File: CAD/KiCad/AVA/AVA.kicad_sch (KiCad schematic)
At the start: 48 parts, among them J1 Conn_01x03_Pin, J10 Conn_01x04_Pin, J2 Conn_01x03_Pin, J3 Conn_01x03_Pin, J4 Conn_01x03_Pin, J5 Conn_01x02_Pin, J6 Conn_01x02_Pin, J7 Conn_01x02_Pin, J8 Conn_01x03_Pin, J9 Conn_01x03_Pin, U1 ESP32-C3-Super-Mini, U2 ESP32-DevKitC

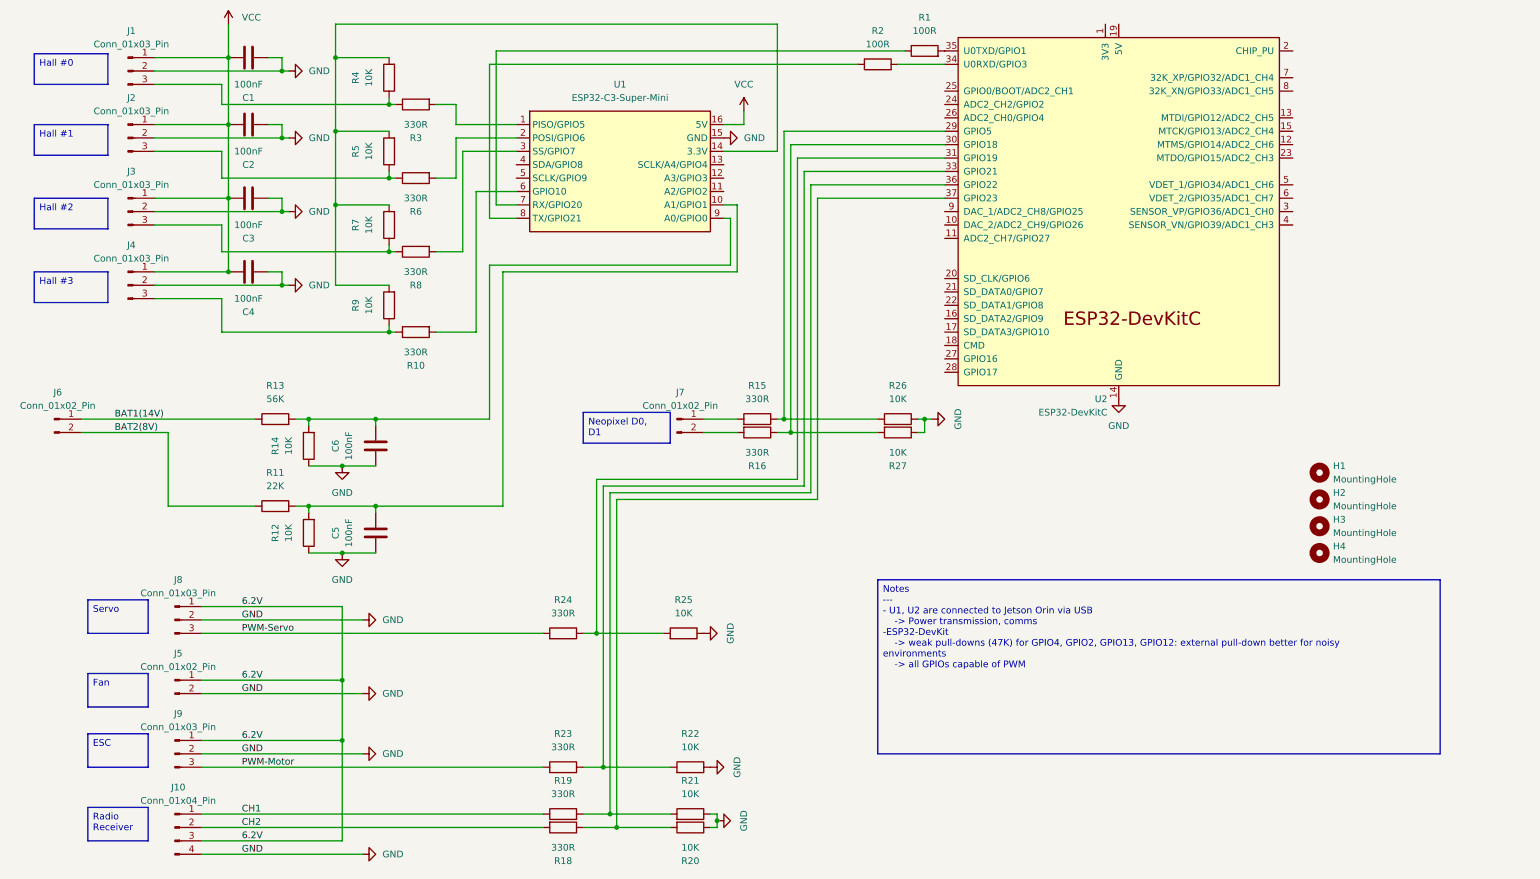
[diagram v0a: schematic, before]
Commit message: ESP32-DevKitC UART pins shared with usb, changing it to GPIO16/17. GPIO5 is strapping pin, changing pwm channels to GPIO4,18,19,20,21,22,23. GPIO4 in RTC-power-domain (touch sensor for deep-sleep mode, using it as normal PWM GPIO
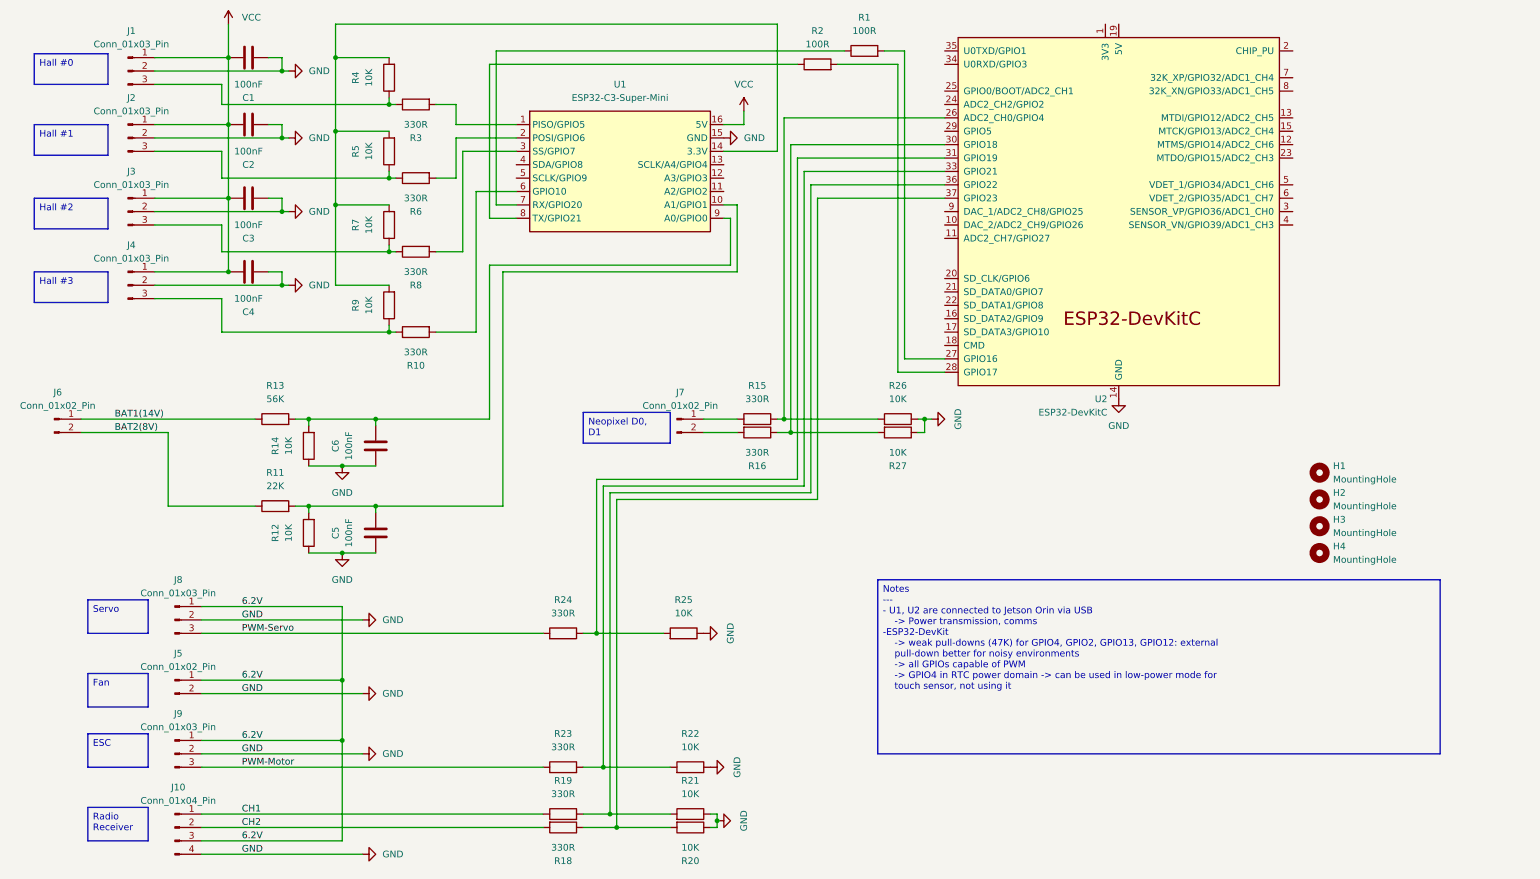
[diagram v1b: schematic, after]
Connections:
- net at R1.2: now also U2.27 (GPIO16); no longer U2.35 (U0TXD/GPIO1)
- net at R15.1, R26.2: now also U2.26 (ADC2_CH0/GPIO4); no longer U2.29 (GPIO5)
- net at R2.2: now also U2.28 (GPIO17); no longer U2.34 (U0RXD/GPIO3)
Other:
- moved on the sheet: R1, R2

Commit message: Added revision on pcb layout and updated 3D view
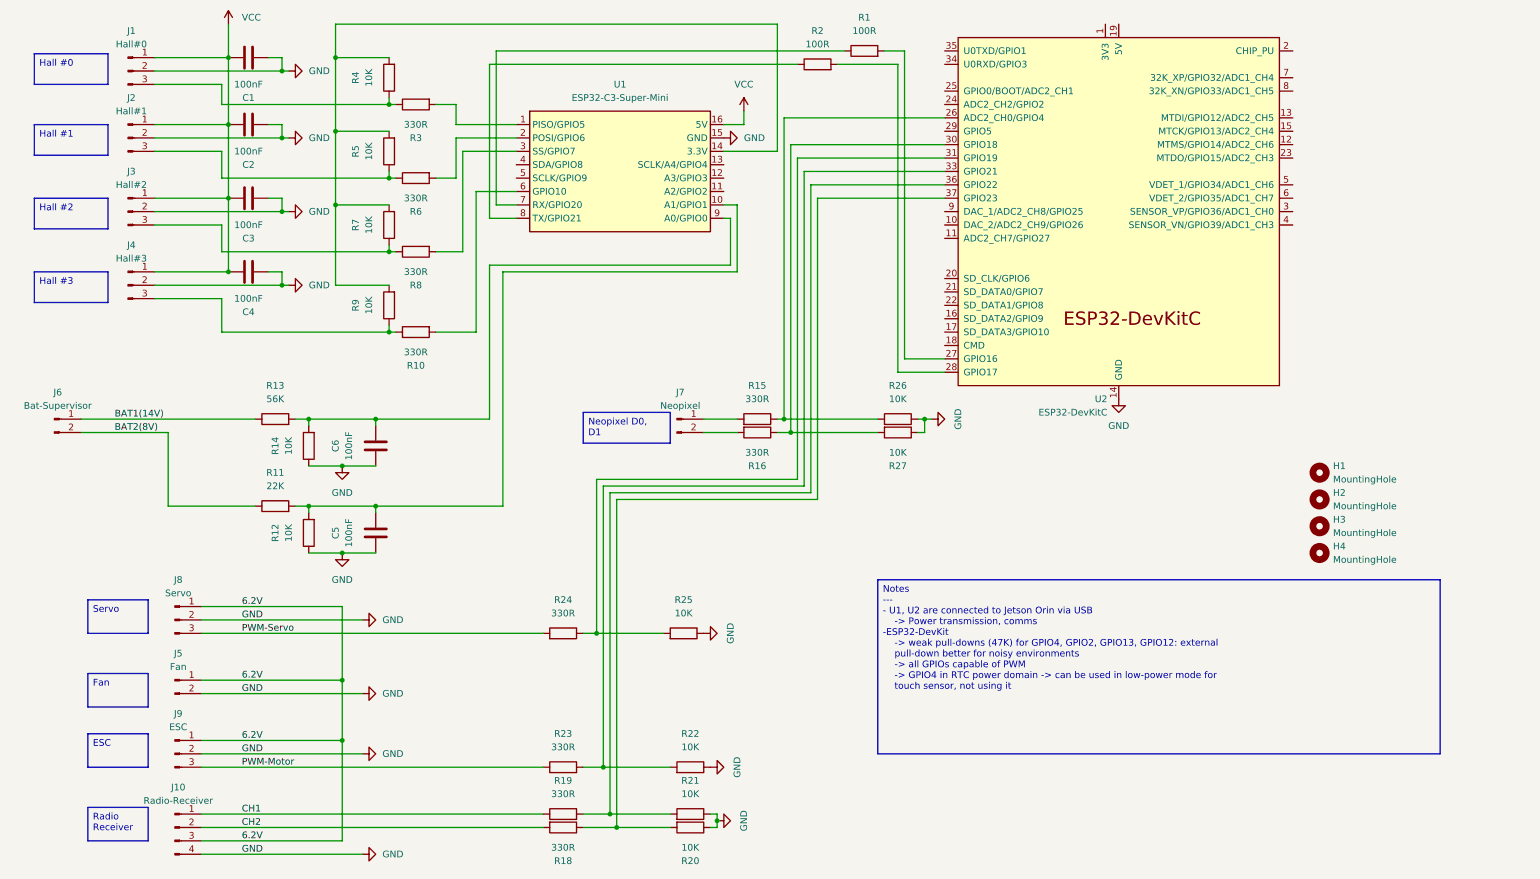
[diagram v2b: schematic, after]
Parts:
- J1: value Conn_01x03_Pin -> Hall#0
- J10: value Conn_01x04_Pin -> Radio-Receiver
- J2: value Conn_01x03_Pin -> Hall#1
- J3: value Conn_01x03_Pin -> Hall#2
- J4: value Conn_01x03_Pin -> Hall#3
- J5: value Conn_01x02_Pin -> Fan
- J6: value Conn_01x02_Pin -> Bat-Supervisor
- J7: value Conn_01x02_Pin -> Neopixel
- J8: value Conn_01x03_Pin -> Servo
- J9: value Conn_01x03_Pin -> ESC
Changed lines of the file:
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@@
 		(title "AVA")
 		(date "0026-04-28")
-		(rev "0")
+		(rev "10")
 	)
 	(text_box "Hall #2"
@@
 			)
 		)
-		(property "Value" "Conn_01x02_Pin"
+		(property "Value" "Fan"
 			(at 45.085 149.86 0)
 			(show_name no)
@@
 			)
 		)
-		(property "Value" "Conn_01x02_Pin"
+		(property "Value" "Neopixel"
 			(at 140.335 100.33 0)
 			(show_name no)
@@
 			)
 		)
-		(property "Value" "Conn_01x03_Pin"
+		(property "Value" "Servo"
 			(at 45.085 135.89 0)
 			(show_name no)
@@
 			)
 		)
-		(property "Value" "Conn_01x03_Pin"
+		(property "Value" "Hall#1"
 			(at 36.195 44.45 0)
 			(show_name no)
@@
 			)
 		)
-		(property "Value" "Conn_01x03_Pin"
+		(property "Value" "ESC"
 			(at 45.085 161.29 0)
 			(show_name no)
@@
 			)
 		)
-		(property "Value" "Conn_01x04_Pin"
+		(property "Value" "Radio-Receiver"
 			(at 45.085 175.26 0)
 			(show_name no)
@@
 			)
 		)
-		(property "Value" "Conn_01x02_Pin"
+		(property "Value" "Bat-Supervisor"
 			(at 22.225 100.33 0)
 			(show_name no)
@@
 			)
 		)
-		(property "Value" "Conn_01x03_Pin"
+		(property "Value" "Hall#0"
 			(at 36.195 31.75 0)
 			(show_name no)
@@
 			)
 		)
-		(property "Value" "Conn_01x03_Pin"
+		(property "Value" "Hall#2"
 			(at 36.195 58.42 0)
 			(show_name no)
@@
 			)
 		)
-		(property "Value" "Conn_01x03_Pin"
+		(property "Value" "Hall#3"
 			(at 36.195 72.39 0)
 			(show_name no)
